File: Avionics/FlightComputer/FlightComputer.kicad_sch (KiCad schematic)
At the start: 35 parts

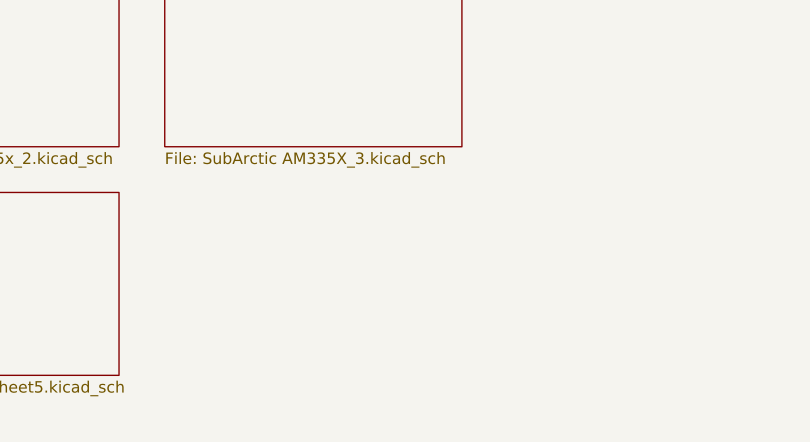
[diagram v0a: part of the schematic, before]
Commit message: Ian Goldberg - Finished the 7th sheet of the Flight Computer schematic.
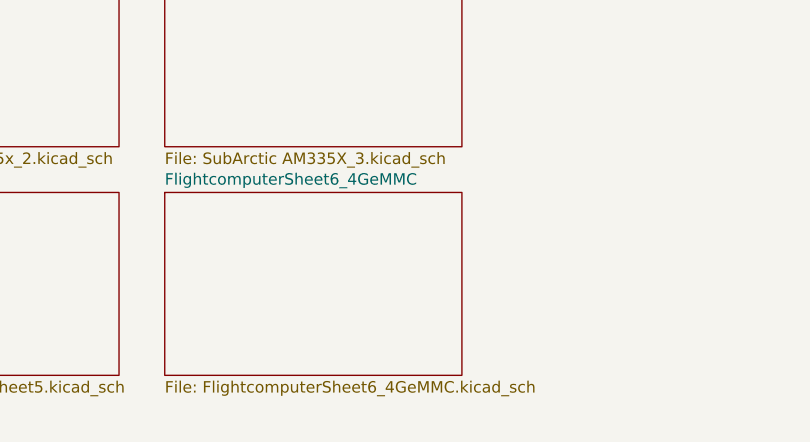
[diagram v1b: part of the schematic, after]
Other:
- added sheet FlightcomputerSheet6_4GeMMC (FlightcomputerSheet6_4GeMMC.kicad_sch)
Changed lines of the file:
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@@
+	)
+	(sheet
+		(at 92.71 168.91)
+		(size 33.02 20.32)
+		(fields_autoplaced yes)
+		(stroke
+			(width 0.1524)
+			(type solid)
+		)
+		(fill
+			(color 0 0 0 0.0000)
+		)
+		(property "Sheetname" "FlightcomputerSheet6_4GeMMC"
+			(at 92.71 168.1984 0)
+			(effects
+				(font
+					(size 1.27 1.27)
+				)
+				(justify left bottom)
+			)
+		)
+		(property "Sheetfile" "FlightcomputerSheet6_4GeMMC.kicad_sch"
+			(at 92.71 189.8146 0)
+			(effects
+				(font
+					(size 1.27 1.27)
+				)
+				(justify left top)
+			)
+		)
+		(property "Field2" ""
+			(at 92.71 168.91 0)
+			(effects
+				(font
+					(size 1.27 1.27)
+				)
+				(hide yes)
+			)
+		)
+		(instances
+			(project "FlightComputer"
+				(path "/80fd70cc-258e-4c36-a149-cd51380d23dc"
+					(page "8")
+				)
+			)
+		)
 	)
 	(sheet

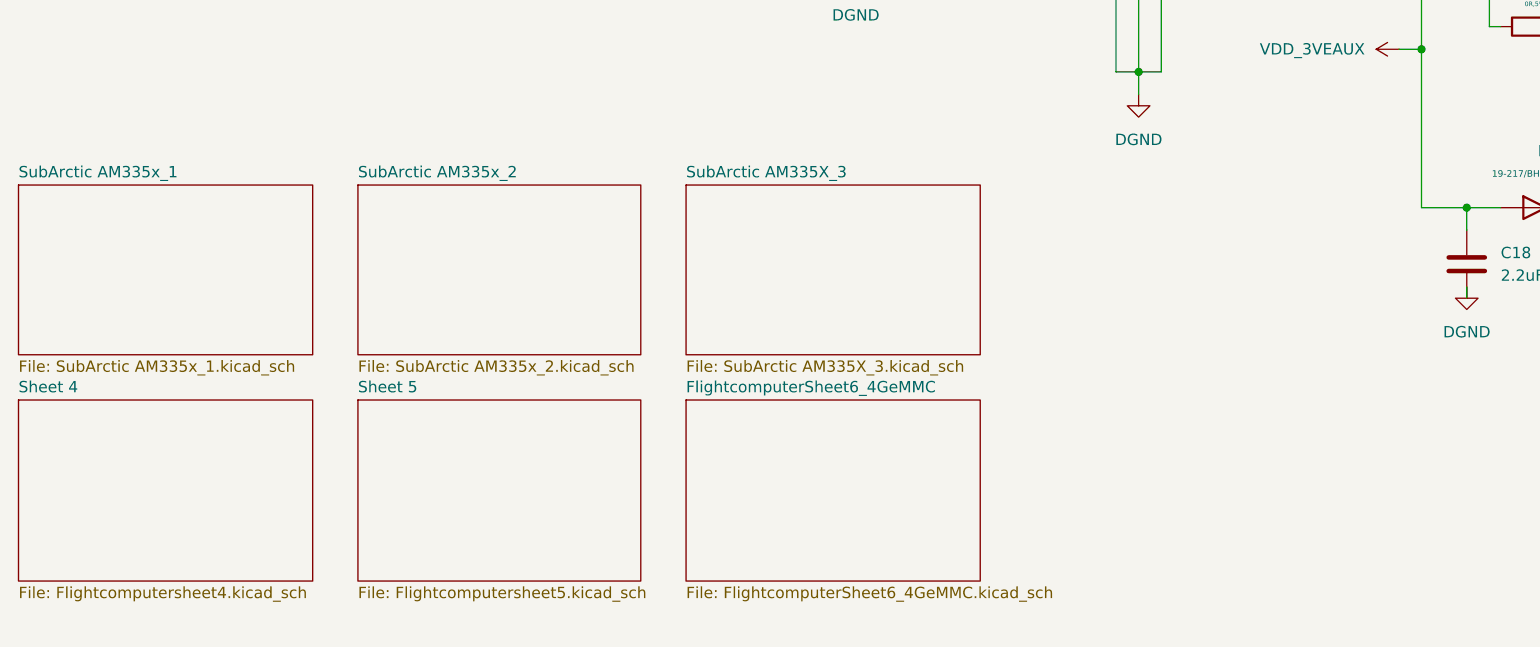
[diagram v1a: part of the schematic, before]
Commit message: Ian Goldberg - Added a 7th sheet to the flight computer schematic
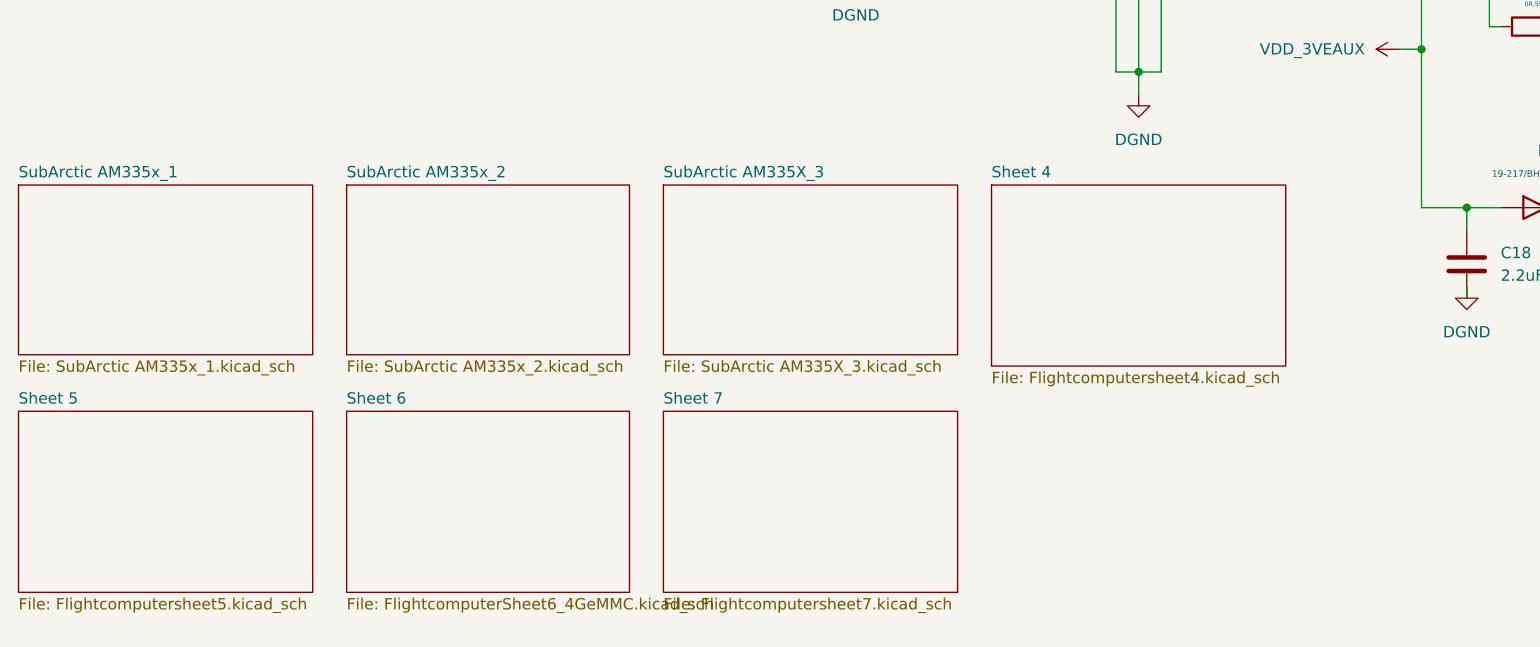
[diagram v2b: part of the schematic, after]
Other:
- sheet FlightcomputerSheet6_4GeMMC renamed Sheet 6
- added sheet Sheet 7 (Flightcomputersheet7.kicad_sch)
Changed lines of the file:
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@@
 	)
 	(sheet
-		(at 92.71 144.78)
+		(at 90.17 144.78)
 		(size 33.02 19.05)
 		(fields_autoplaced yes)
@@
 		)
 		(property "Sheetname" "SubArctic AM335X_3"
-			(at 92.71 144.0684 0)
+			(at 90.17 144.0684 0)
 			(effects
 				(font
@@
 		)
 		(property "Sheetfile" "SubArctic AM335X_3.kicad_sch"
-			(at 92.71 164.4146 0)
+			(at 90.17 164.4146 0)
 			(effects
 				(font
@@
 	)
 	(sheet
-		(at 17.78 168.91)
+		(at 127 144.78)
 		(size 33.02 20.32)
 		(fields_autoplaced yes)
@@
 		)
 		(property "Sheetname" "Sheet 4"
-			(at 17.78 168.1984 0)
+			(at 127 144.0684 0)
 			(effects
 				(font
@@
 		)
 		(property "Sheetfile" "Flightcomputersheet4.kicad_sch"
-			(at 17.78 189.8146 0)
+			(at 127 165.6846 0)
 			(effects
 				(font
@@
 	)
 	(sheet
-		(at 92.71 168.91)
+		(at 54.61 170.18)
+		(size 31.75 20.32)
+		(fields_autoplaced yes)
+		(stroke
+			(width 0.1524)
+			(type solid)
+		)
+		(fill
+			(color 0 0 0 0.0000)
+		)
+		(property "Sheetname" "Sheet 6"
+			(at 54.61 169.4684 0)
+			(effects
+				(font
+					(size 1.27 1.27)
+				)
+				(justify left bottom)
+			)
+		)
+		(property "Sheetfile" "FlightcomputerSheet6_4GeMMC.kicad_sch"
+			(at 54.61 191.0846 0)
+			(effects
+				(font
+					(size 1.27 1.27)
+				)
+				(justify left top)
+			)
+		)
+		(property "Field2" ""
+			(at 54.61 170.18 0)
+			(effects
+				(font
+					(size 1.27 1.27)
+				)
+				(hide yes)
+			)
+		)
+		(instances
+			(project "FlightComputer"
+				(path "/80fd70cc-258e-4c36-a149-cd51380d23dc"
+					(page "8")
+				)
+			)
+		)
+	)
+	(sheet
+		(at 17.78 170.18)
 		(size 33.02 20.32)
 		(fields_autoplaced yes)
@@
 			(color 0 0 0 0.0000)
 		)
-		(property "Sheetname" "FlightcomputerSheet6_4GeMMC"
-			(at 92.71 168.1984 0)
-			(effects
-				(font
-					(size 1.27 1.27)
-				)
-				(justify left bottom)
-			)
-		)
-		(property "Sheetfile" "FlightcomputerSheet6_4GeMMC.kicad_sch"
-			(at 92.71 189.8146 0)
-			(effects
-				(font
-					(size 1.27 1.27)
-				)
-				(justify left top)
-			)
-		)
-		(property "Field2" ""
-			(at 92.71 168.91 0)
-			(effects
-				(font
-					(size 1.27 1.27)
-				)
-				(hide yes)
-			)
-		)
-		(instances
-			(project "FlightComputer"
-				(path "/80fd70cc-258e-4c36-a149-cd51380d23dc"
-					(page "8")
-				)
-			)
-		)
-	)
-	(sheet
-		(at 55.88 168.91)
-		(size 31.75 20.32)
-		(fields_autoplaced yes)
-		(stroke
-			(width 0.1524)
-			(type solid)
-		)
-		(fill
-			(color 0 0 0 0.0000)
-		)
 		(property "Sheetname" "Sheet 5"
-			(at 55.88 168.1984 0)
+			(at 17.78 169.4684 0)
 			(effects
 				(font
@@
 		)
 		(property "Sheetfile" "Flightcomputersheet5.kicad_sch"
-			(at 55.88 189.8146 0)
-			(effects
-				(font
-					(size 1.27 1.27)
-				)
-				(justify left top)
-			)
-		)
-		(property "Field2" ""
-			(at 55.88 168.91 0)
+			(at 17.78 191.0846 0)
+			(effects
+				(font
+					(size 1.27 1.27)
+				)
+				(justify left top)
+			)
+		)
+		(property "Field2" ""
+			(at 17.78 170.18 0)
 			(effects
 				(font
@@
 	)
 	(sheet
-		(at 55.88 144.78)
+		(at 90.17 170.18)
+		(size 33.02 20.32)
+		(fields_autoplaced yes)
+		(stroke
+			(width 0.1524)
+			(type solid)
+		)
+		(fill
+			(color 0 0 0 0.0000)
+		)
+		(property "Sheetname" "Sheet 7"
+			(at 90.17 169.4684 0)
+			(effects
+				(font
+					(size 1.27 1.27)
+				)
+				(justify left bottom)
+			)
+		)
+		(property "Sheetfile" "Flightcomputersheet7.kicad_sch"
+			(at 90.17 191.0846 0)
+			(effects
+				(font
+					(size 1.27 1.27)
+				)
+				(justify left top)
+			)
+		)
+		(property "Field2" ""
+			(at 90.17 170.18 0)
+			(effects
+				(font
+					(size 1.27 1.27)
+				)
+				(hide yes)
+			)
+		)
+		(instances
+			(project "FlightComputer"
+				(path "/80fd70cc-258e-4c36-a149-cd51380d23dc"
+					(page "8")
+				)
+			)
+		)
+	)
+	(sheet
+		(at 54.61 144.78)
 		(size 31.75 19.05)
 		(fields_autoplaced yes)
@@
 		)
 		(property "Sheetname" "SubArctic AM335x_2"
-			(at 55.88 144.0684 0)
+			(at 54.61 144.0684 0)
 			(effects
 				(font
@@
 		)
 		(property "Sheetfile" "SubArctic AM335x_2.kicad_sch"
-			(at 55.88 164.4146 0)
-			(effects
-				(font
-					(size 1.27 1.27)
-				)
-				(justify left top)
-			)
-		)
-		(property "Field2" ""
-			(at 55.88 144.78 0)
-			(effects
-				(font
+			(at 54.61 164.4146 0)
+			(effects
+				(font
+					(size 1.27 1.27)
+				)
+				(justify left top)
+			)
+		)
+		(property "Field2" ""
+			(at 54.61 144.78 0)
+			(effects
+				(font
